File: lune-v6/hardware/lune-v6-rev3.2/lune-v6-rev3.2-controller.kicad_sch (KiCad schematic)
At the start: 19 parts, among them SW1 RESET, SW2 BOOT, U1 ESP32-S3-WROOM-1-N8R8, U24 XL74HC4514D, U25 SN74LVC1G00DBVR

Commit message: Refactor code structure for improved readability and maintainability
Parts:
- C13: value 10u -> 10u 16V; footprint Capacitor_SMD:C_0805_2012Metric -> Capacitor_SMD:C_0603_1608Metric; Dielectric (none) -> X5R_RATIFIED_VERIFY_EFFECTIVE_C_AT_3V3; LCSC C380346 -> C18164635; MPN TCC0805X7R106K100FT -> TCC0603X5R106K160CT
- U25: value SN74LVC1G00DBVR -> SN74LVC1G00DCKR; footprint Package_TO_SOT_SMD:SOT-23-5 -> Package_TO_SOT_SMD:SOT-353_SC-70-5; LCSC C7826 -> C8185; MPN SN74LVC1G00DBVR -> SN74LVC1G00DCKR

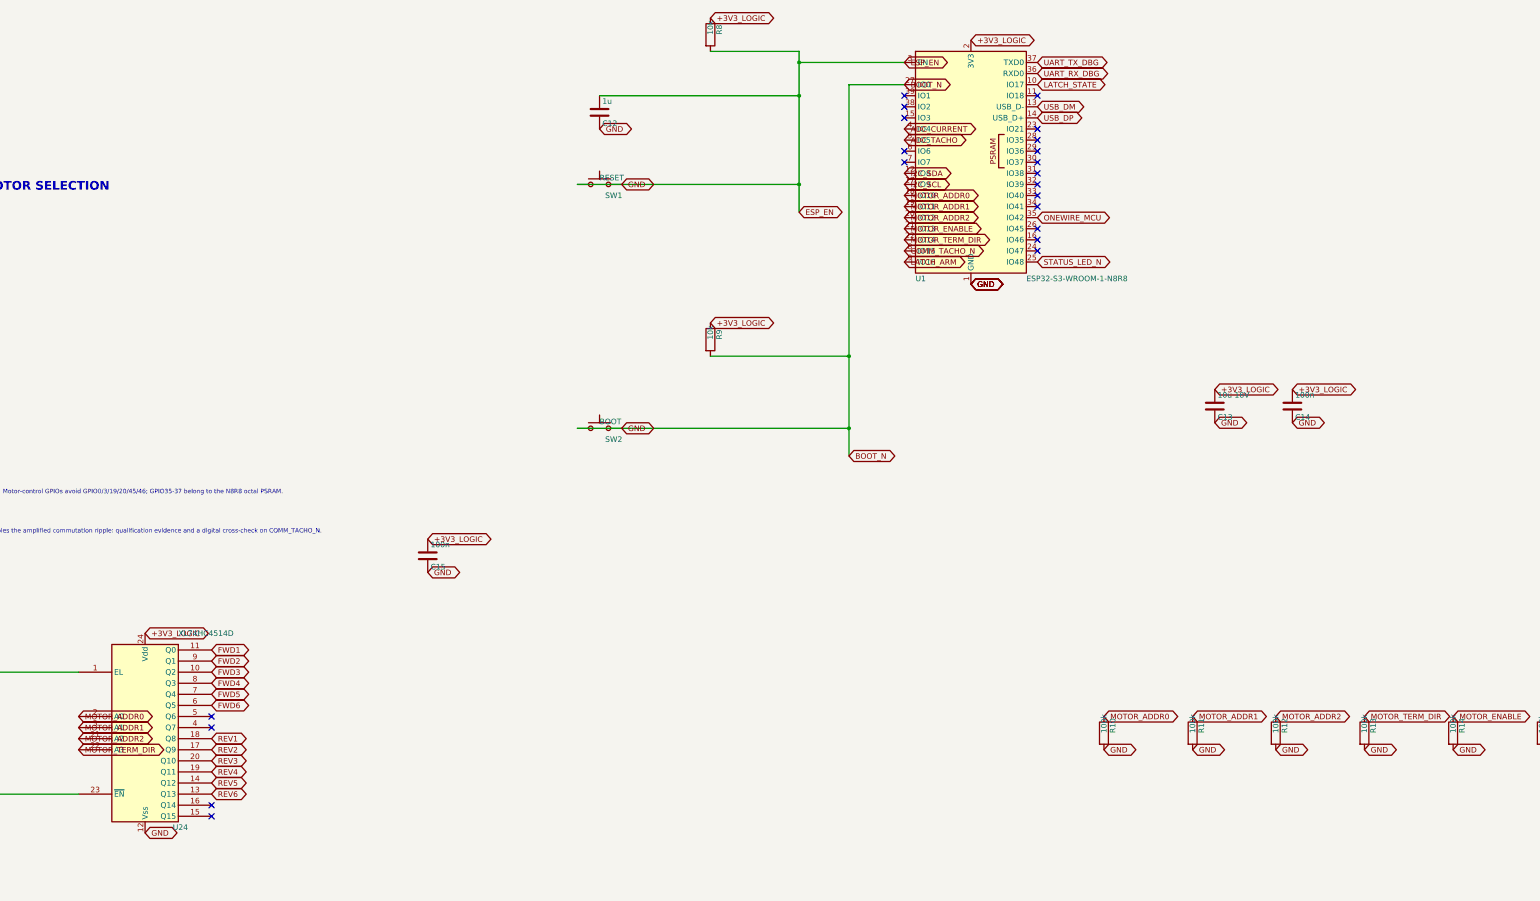
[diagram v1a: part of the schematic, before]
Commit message: Add placement floorplan SVG and geometry JSON for Lune V6 rev3.2
- Introduced a new SVG file for the component placement floorplan, detailing the layout and dimensions of the Lune V6 rev3.2 hardware.
- Added a JSON file containing the geometric coordinates for each component, including reference designators and their respective positions on the board.
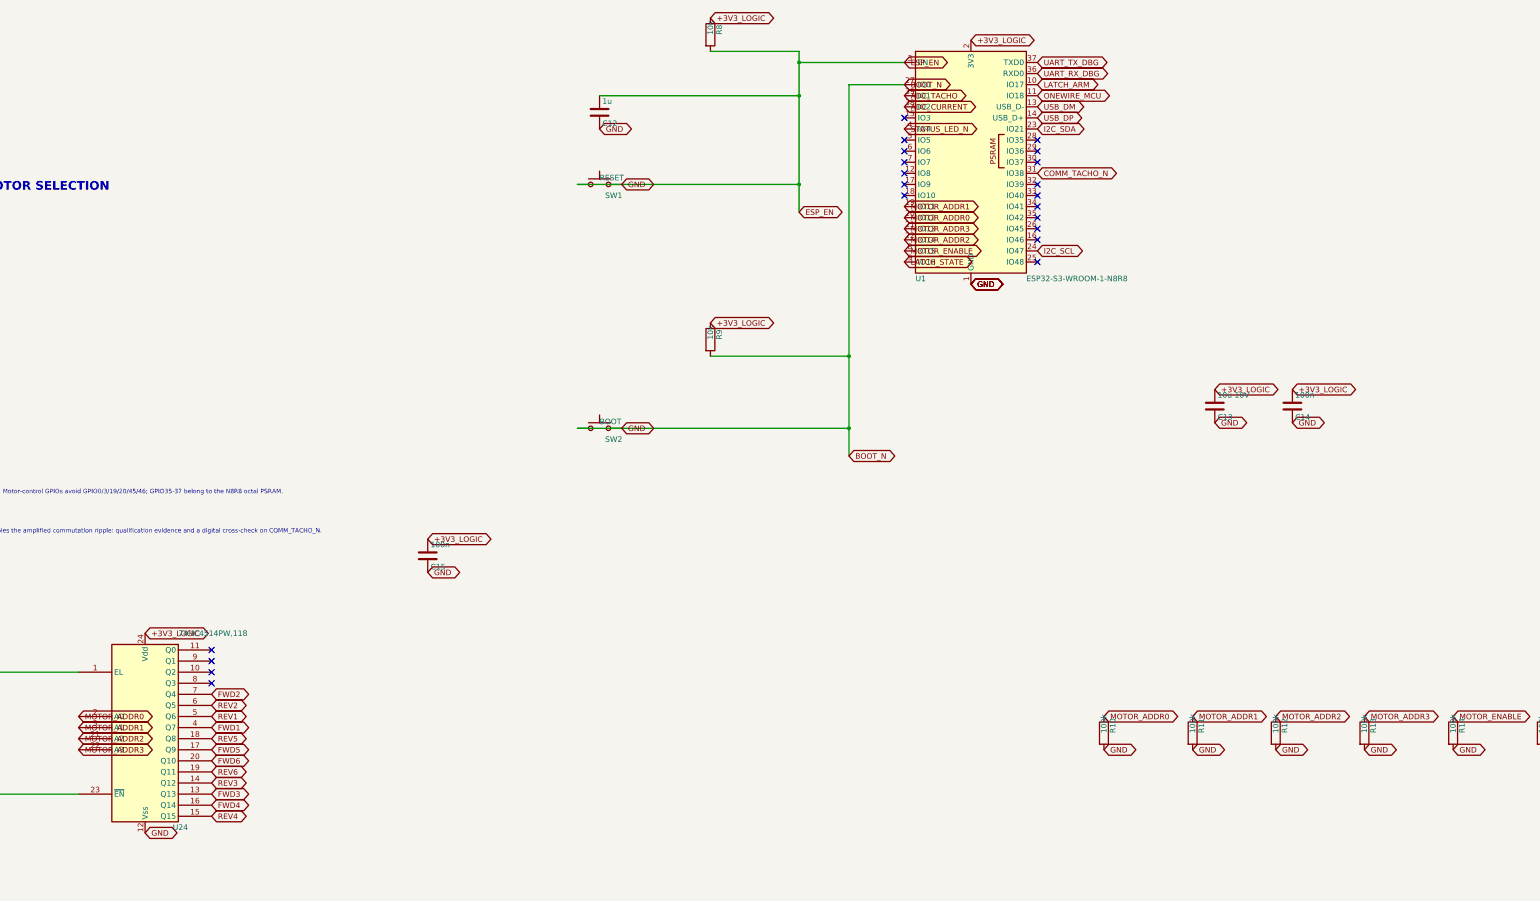
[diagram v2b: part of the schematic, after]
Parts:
- U24: value XL74HC4514D -> 74HC4514PW,118; footprint Package_SO:SOIC-24W_7.5x15.4mm_P1.27mm -> Package_SO:TSSOP-24_4.4x7.8mm_P0.65mm; LCSC C50202050 -> C58910; MPN XL74HC4514D -> 74HC4514PW,118
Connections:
- net ADC_CURRENT: now also U1.38 (IO2); no longer U1.4 (IO4)
- net ADC_TACHO: now also U1.39 (IO1); no longer U1.5 (IO5)
- net COMM_TACHO_N: now also U1.31 (IO38); no longer U1.8 (IO15)
- net FWD1: now also U24.4 (Q7); no longer U24.11 (Q0)
- net FWD2: now also U24.7 (Q4); no longer U24.9 (Q1)
- net FWD3: now also U24.13 (Q13); no longer U24.10 (Q2)
- net FWD4: now also U24.16 (Q14); no longer U24.8 (Q3)
- net FWD5: now also U24.17 (Q9); no longer U24.7 (Q4)
- net FWD6: now also U24.20 (Q10); no longer U24.6 (Q5)
- net I2C_SCL: now also U1.24 (IO47); no longer U1.17 (IO9)
- net I2C_SDA: now also U1.23 (IO21); no longer U1.12 (IO8)
- net LATCH_ARM: now also U1.10 (IO17); no longer U1.9 (IO16)
- net LATCH_STATE: now also U1.9 (IO16); no longer U1.10 (IO17)
- net MOTOR_ADDR0: now also U1.20 (IO12); no longer U1.18 (IO10)
- net MOTOR_ADDR2: now also U1.22 (IO14); no longer U1.20 (IO12)
- net MOTOR_ENABLE: now also U1.8 (IO15); no longer U1.21 (IO13)
- net ONEWIRE_MCU: now also U1.11 (IO18); no longer U1.35 (IO42)
- net REV1: now also U24.5 (Q6); no longer U24.18 (Q8)
- net REV2: now also U24.6 (Q5); no longer U24.17 (Q9)
- net REV3: now also U24.14 (Q12); no longer U24.20 (Q10)
- net REV4: now also U24.15 (Q15); no longer U24.19 (Q11)
- net REV5: now also U24.18 (Q8); no longer U24.14 (Q12)
- net REV6: now also U24.19 (Q11); no longer U24.13 (Q13)
- net STATUS_LED_N: now also U1.4 (IO4); no longer U1.25 (IO48)
- net MOTOR_TERM_DIR renamed MOTOR_ADDR3
- net MOTOR_ADDR3: now also U1.21 (IO13); no longer U1.22 (IO14)

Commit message: Refactor code structure and remove redundant changes
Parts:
- added R53, R54: 1k, Resistor_SMD:R_0603_1608Metric, symbol Device:R
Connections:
- net MOTOR_ENABLE: now also U1.11 (IO18); no longer U1.8 (IO15)
- net ONEWIRE_MCU: now also U1.12 (IO8); no longer U1.11 (IO18)
- net UART_RX_DBG: now also R54.2; no longer U1.36 (RXD0)
- net UART_TX_DBG: now also R53.2; no longer U1.37 (TXD0)
- new net UART_RX_MCU: R54.1, U1.36 (RXD0)
- new net UART_TX_MCU: R53.1, U1.37 (TXD0)
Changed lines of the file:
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@@
 		(instances
 			(project "Controller and Safety"
-				(path "/14c3f1d6-aa79-4a38-8fe9-83d22b363173"
+				(path "/5dce06be-ae34-4673-8683-986019f80975"
 					(reference "U1")
+					(unit 1)
+				)
+			)
+		)
+	)
+	(symbol
+		(lib_id "Device:R")
+		(at 500.38 100.33 0)
+		(unit 1)
+		(exclude_from_sim no)
+		(in_bom yes)
+		(on_board yes)
+		(dnp no)
+		(fields_autoplaced no)
+		(property "Reference" "R53"
+			(at 502.412 100.33 90)
+			(effects
+				(font
+					(size 1.27 1.27)
+				)
+				(justify left)
+			)
+		)
+		(property "Value" "1k"
+			(at 500.38 100.33 90)
+			(effects
+				(font
+					(size 1.27 1.27)
+				)
+				(justify left)
+			)
+		)
+		(property "Footprint" "Resistor_SMD:R_0603_1608Metric"
+			(at 498.602 100.33 90)
+			(effects
+				(font
+					(size 1.27 1.27)
+				)
+				(hide yes)
+			)
+		)
+		(property "MPN" "RC0603FR-071KL"
+			(at 502.92 105.4099 0)
+			(effects
+				(font
+					(size 1.27 1.27)
+				)
+				(hide yes)
+			)
+		)
+		(property "LCSC" "C22548"
+			(at 502.92 105.4099 0)
+			(effects
+				(font
+					(size 1.27 1.27)
+				)
+				(hide yes)
+			)
+		)
+		(pin "1"
+		)
+		(pin "2"
+		)
+		(instances
+			(project "Controller and Safety"
+				(path "/5dce06be-ae34-4673-8683-986019f80975"
+					(reference "R53")
+					(unit 1)
+				)
+			)
+		)
+	)
+	(symbol
+		(lib_id "Device:R")
+		(at 500.38 139.7 0)
+		(unit 1)
+		(exclude_from_sim no)
+		(in_bom yes)
+		(on_board yes)
+		(dnp no)
+		(fields_autoplaced no)
+		(property "Reference" "R54"
+			(at 502.412 139.7 90)
+			(effects
+				(font
+					(size 1.27 1.27)
+				)
+				(justify left)
+			)
+		)
+		(property "Value" "1k"
+			(at 500.38 139.7 90)
+			(effects
+				(font
+					(size 1.27 1.27)
+				)
+				(justify left)
+			)
+		)
+		(property "Footprint" "Resistor_SMD:R_0603_1608Metric"
+			(at 498.602 139.7 90)
+			(effects
+				(font
+					(size 1.27 1.27)
+				)
+				(hide yes)
+			)
+		)
+		(property "MPN" "RC0603FR-071KL"
+			(at 502.92 144.7799 0)
+			(effects
+				(font
+					(size 1.27 1.27)
+				)
+				(hide yes)
+			)
+		)
+		(property "LCSC" "C22548"
+			(at 502.92 144.7799 0)
+			(effects
+				(font
+					(size 1.27 1.27)
+				)
+				(hide yes)
+			)
+		)
+		(pin "1"
+		)
+		(pin "2"
+		)
+		(instances
+			(project "Controller and Safety"
+				(path "/5dce06be-ae34-4673-8683-986019f80975"
+					(reference "R54")
 					(unit 1)
 				)
@@
 		(instances
 			(project "Controller and Safety"
-				(path "/14c3f1d6-aa79-4a38-8fe9-83d22b363173"
+				(path "/5dce06be-ae34-4673-8683-986019f80975"
 					(reference "R8")
 					(unit 1)
@@
 		(instances
 			(project "Controller and Safety"
-				(path "/14c3f1d6-aa79-4a38-8fe9-83d22b363173"
+				(path "/5dce06be-ae34-4673-8683-986019f80975"
 					(reference "C12")
 					(unit 1)
@@
 		(instances
 			(project "Controller and Safety"
-				(path "/14c3f1d6-aa79-4a38-8fe9-83d22b363173"
+				(path "/5dce06be-ae34-4673-8683-986019f80975"
 					(reference "SW1")
 					(unit 1)
@@
 		(instances
 			(project "Controller and Safety"
-				(path "/14c3f1d6-aa79-4a38-8fe9-83d22b363173"
+				(path "/5dce06be-ae34-4673-8683-986019f80975"
 					(reference "R9")
 					(unit 1)
@@
 		(instances
 			(project "Controller and Safety"
-				(path "/14c3f1d6-aa79-4a38-8fe9-83d22b363173"
+				(path "/5dce06be-ae34-4673-8683-986019f80975"
 					(reference "SW2")
 					(unit 1)
@@
 		(instances
 			(project "Controller and Safety"
-				(path "/14c3f1d6-aa79-4a38-8fe9-83d22b363173"
+				(path "/5dce06be-ae34-4673-8683-986019f80975"
 					(reference "C13")
 					(unit 1)
@@
 		(instances
 			(project "Controller and Safety"
-				(path "/14c3f1d6-aa79-4a38-8fe9-83d22b363173"
+				(path "/5dce06be-ae34-4673-8683-986019f80975"
 					(reference "C14")
 					(unit 1)
@@
 		(instances
 			(project "Controller and Safety"
-				(path "/14c3f1d6-aa79-4a38-8fe9-83d22b363173"
+				(path "/5dce06be-ae34-4673-8683-986019f80975"
 					(reference "U24")
 					(unit 1)
@@
 		(instances
 			(project "Controller and Safety"
-				(path "/14c3f1d6-aa79-4a38-8fe9-83d22b363173"
+				(path "/5dce06be-ae34-4673-8683-986019f80975"
 					(reference "C15")
 					(unit 1)
@@
 		(instances
 			(project "Controller and Safety"
-				(path "/14c3f1d6-aa79-4a38-8fe9-83d22b363173"
+				(path "/5dce06be-ae34-4673-8683-986019f80975"
 					(reference "U25")
 					(unit 1)
@@
 		(instances
 			(project "Controller and Safety"
-				(path "/14c3f1d6-aa79-4a38-8fe9-83d22b363173"
+				(path "/5dce06be-ae34-4673-8683-986019f80975"
 					(reference "C16")
 					(unit 1)
@@
 		(instances
 			(project "Controller and Safety"
-				(path "/14c3f1d6-aa79-4a38-8fe9-83d22b363173"
+				(path "/5dce06be-ae34-4673-8683-986019f80975"
 					(reference "R10")
 					(unit 1)
@@
 		(instances
 			(project "Controller and Safety"
-				(path "/14c3f1d6-aa79-4a38-8fe9-83d22b363173"
+				(path "/5dce06be-ae34-4673-8683-986019f80975"
 					(reference "R11")
 					(unit 1)
@@
 		(instances
 			(project "Controller and Safety"
-				(path "/14c3f1d6-aa79-4a38-8fe9-83d22b363173"
+				(path "/5dce06be-ae34-4673-8683-986019f80975"
 					(reference "R12")
 					(unit 1)
@@
 		(instances
 			(project "Controller and Safety"
-				(path "/14c3f1d6-aa79-4a38-8fe9-83d22b363173"
+				(path "/5dce06be-ae34-4673-8683-986019f80975"
 					(reference "R13")
 					(unit 1)
@@
 		(instances
 			(project "Controller and Safety"
-				(path "/14c3f1d6-aa79-4a38-8fe9-83d22b363173"
+				(path "/5dce06be-ae34-4673-8683-986019f80975"
 					(reference "R14")
 					(unit 1)
@@
 		(instances
 			(project "Controller and Safety"
-				(path "/14c3f1d6-aa79-4a38-8fe9-83d22b363173"
+				(path "/5dce06be-ae34-4673-8683-986019f80975"
 					(reference "R15")
 					(unit 1)
@@
 		(instances
 			(project "Controller and Safety"
-				(path "/14c3f1d6-aa79-4a38-8fe9-83d22b363173"
+				(path "/5dce06be-ae34-4673-8683-986019f80975"
 					(reference "TP4")
 					(unit 1)
@@
 	(global_label "MOTOR_ENABLE"
 		(shape bidirectional)
-		(at 284.48 139.7 0)
+		(at 314.96 104.14 0)
 		(effects
 			(font
@@
 	(global_label "ONEWIRE_MCU"
 		(shape bidirectional)
-		(at 314.96 104.14 0)
+		(at 284.48 121.92 0)
 		(effects
 			(font
@@
 		)
 	)
+	(global_label "UART_RX_MCU"
+		(shape bidirectional)
+		(at 314.96 99.06 0)
+		(effects
+			(font
+				(size 1.27 1.27)
+			)
+			(justify left bottom)
+		)
+	)
+	(global_label "UART_TX_MCU"
+		(shape bidirectional)
+		(at 314.96 96.52 0)
+		(effects
+			(font
+				(size 1.27 1.27)
+			)
+			(justify left bottom)
+		)
+	)
+	(global_label "UART_TX_MCU"
+		(shape bidirectional)
+		(at 500.38 96.52 0)
+		(effects
+			(font
+				(size 1.27 1.27)
+			)
+			(justify left bottom)
+		)
+	)
+	(global_label "UART_TX_DBG"
+		(shape bidirectional)
+		(at 500.38 104.14 0)
+		(effects
+			(font
+				(size 1.27 1.27)
+			)
+			(justify left bottom)
+		)
+	)
+	(global_label "UART_RX_MCU"
+		(shape bidirectional)
+		(at 500.38 135.89 0)
+		(effects
+			(font
+				(size 1.27 1.27)
+			)
+			(justify left bottom)
+		)
+	)
 	(global_label "UART_RX_DBG"
 		(shape bidirectional)
-		(at 314.96 99.06 0)
-		(effects
-			(font
-				(size 1.27 1.27)
-			)
-			(justify left bottom)
-		)
-	)
-	(global_label "UART_TX_DBG"
-		(shape bidirectional)
-		(at 314.96 96.52 0)
+		(at 500.38 143.51 0)
 		(effects
 			(font
@@
 	)
 	(no_connect
-		(at 284.48 121.92)
+		(at 284.48 139.7)
 	)
 	(no_connect
